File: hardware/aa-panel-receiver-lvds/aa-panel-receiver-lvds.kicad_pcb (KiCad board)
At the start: 2 copper layers, 95.4 x 54 mm, 96 parts, among them CN101 Conn_01x02, CN102 Conn_01x02, CN201 8P8C, CN202 Conn_01x08, CN251 Conn_01x08, CN301 8P8C, CN302 Conn_01x08, CN351 Conn_01x08, U101 CRE1S0505S3C, U201 ST26C32, U202 Si8640EB-B-IU, U301 ST26C32, U302 Si8640EB-B-IU

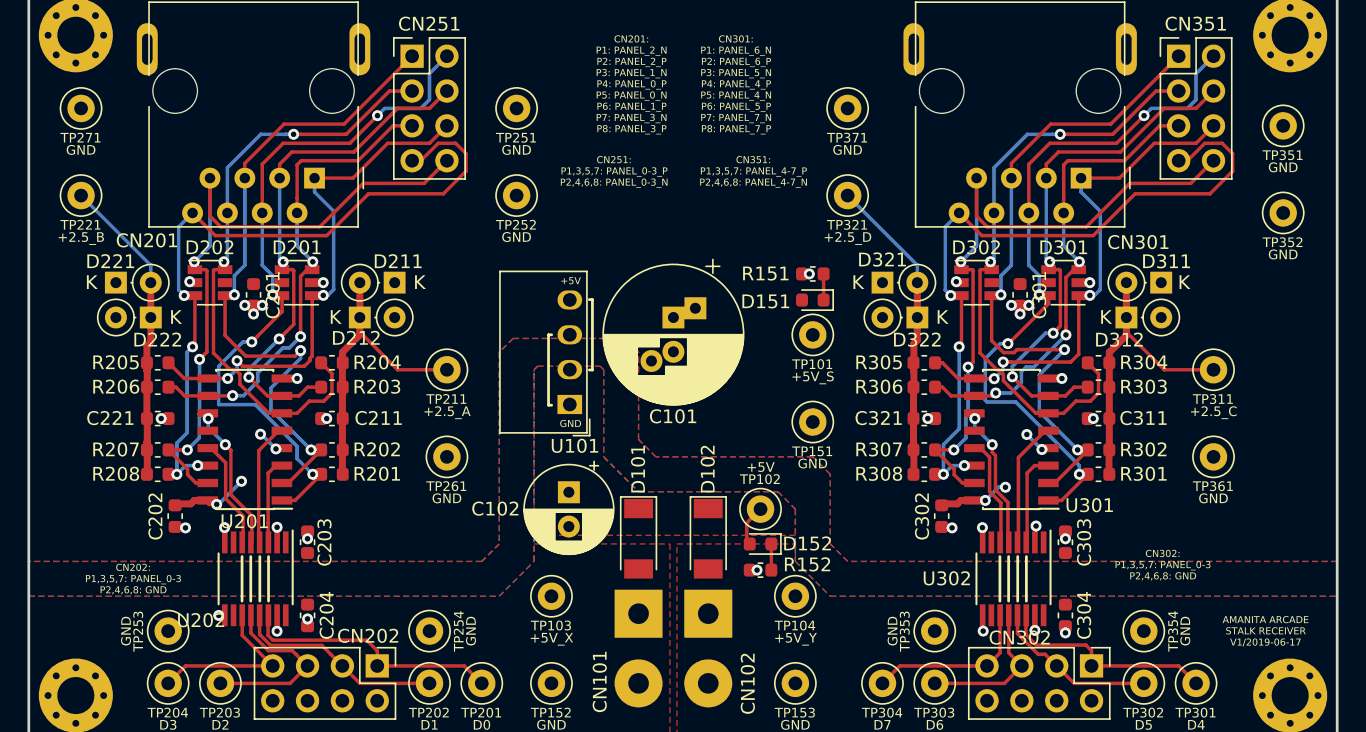
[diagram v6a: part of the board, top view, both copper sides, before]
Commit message: Final designs and actual sent gerbers for first for-real run
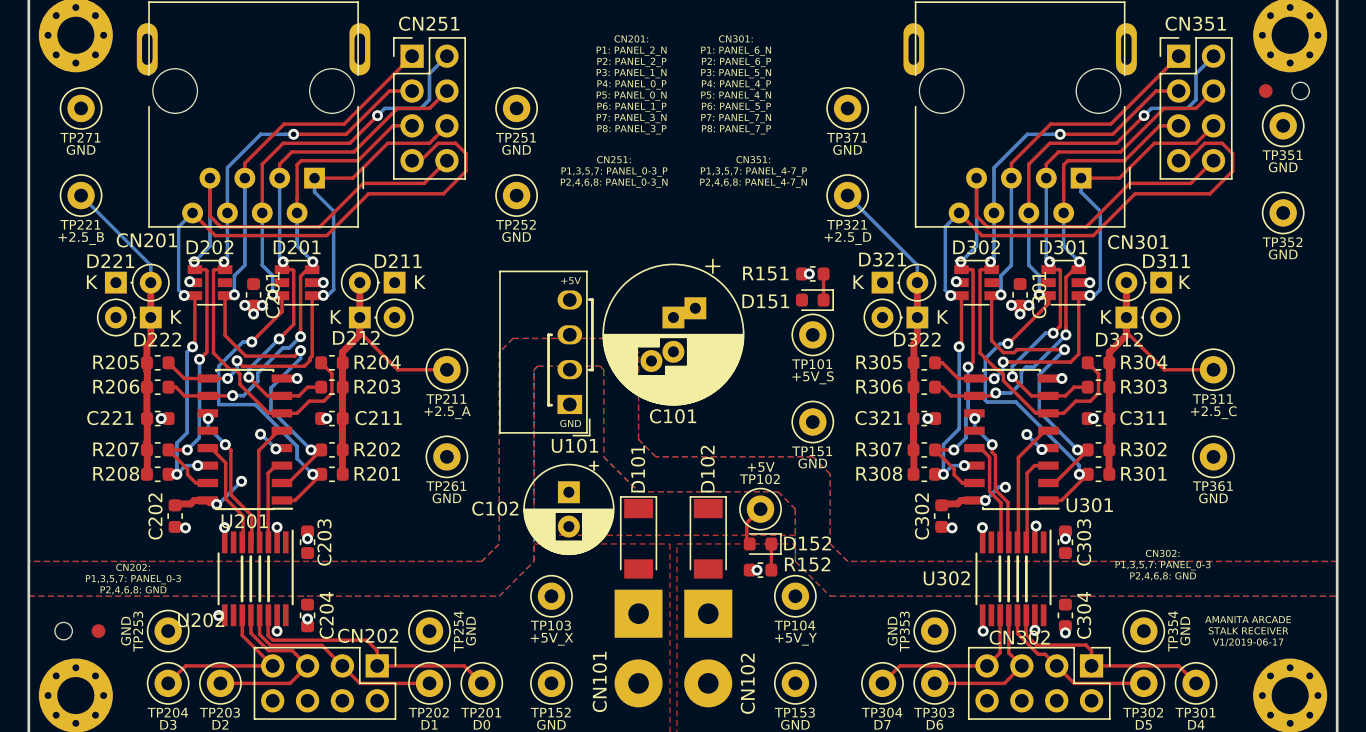
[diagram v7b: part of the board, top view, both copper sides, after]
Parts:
- added FD1: Fiducial, Fiducial:Fiducial_1mm_Dia_2.54mm_Outer_CopperTop, F.Cu at (96.5, 96.5)
- added FD2: Fiducial, Fiducial:Fiducial_1mm_Dia_2.54mm_Outer_CopperTop, F.Cu at (181.6, 57.1)
- added FD5: Fiducial, aa-shared:StencilAlignment_1.27mm, F.Cu at (94.0, 96.5)
- added FD6: Fiducial, aa-shared:StencilAlignment_1.27mm, F.Cu at (184.2, 57.1)
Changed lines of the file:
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@@
     (tracks 742)
     (zones 0)
-    (modules 96)
+    (modules 100)
     (nets 47)
   )
@@
     (uvia_drill 0.1)
   )
+  (module aa-shared:StencilAlignment_1.27mm (layer F.Cu)
+    (at 184.15 57.15)
+    (fp_text reference FD6 (at 0 -2.032) (layer F.SilkS) hide
+      (effects (font (size 1 1) (thickness 0.15)))
+    )
+    (fp_text value Fiducial (at 0 2.667) (layer F.Fab)
+      (effects (font (size 1 1) (thickness 0.15)))
+    )
+    (pad "" np_thru_hole circle (at 0 0) (size 1.27 1.27) (drill 1.27) (layers *.Cu *.Paste *.Mask)
+      (solder_paste_margin 0.00254))
+  )
+  (module Fiducial:Fiducial_1mm_Dia_2.54mm_Outer_CopperTop (layer F.Cu)
+    (at 181.61 57.15)
+    (descr "Circular Fiducial, 1mm bare copper top, 2.54mm keepout")
+    (tags fiducial)
+    (attr smd)
+    (fp_text reference FD2 (at 0 -2.5) (layer F.SilkS) hide
+      (effects (font (size 1 1) (thickness 0.15)))
+    )
+    (fp_text value Fiducial (at 0 2.5) (layer F.Fab)
+      (effects (font (size 1 1) (thickness 0.15)))
+    )
+    (fp_text user %R (at 0 0) (layer F.Fab)
+      (effects (font (size 1 1) (thickness 0.15)))
+    )
+    (fp_circle (center 0 0) (end 1.55 0) (layer F.CrtYd) (width 0.05))
+    (pad "" smd circle (at 0 0) (size 1 1) (layers F.Cu F.Mask)
+      (solder_mask_margin 0.77) (clearance 0.77))
+  )
   (module aa-shared:TestPoint_Loop_D1.80mm_Drill1.0mm_Beaded (layer F.Cu)
     (at 147.32 93.98)
@@
     )
   )
+  (module Fiducial:Fiducial_1mm_Dia_2.54mm_Outer_CopperTop (layer F.Cu)
+    (at 96.52 96.52)
+    (descr "Circular Fiducial, 1mm bare copper top, 2.54mm keepout")
+    (tags fiducial)
+    (attr smd)
+    (fp_text reference FD1 (at 0 -2.5) (layer F.SilkS) hide
+      (effects (font (size 1 1) (thickness 0.15)))
+    )
+    (fp_text value Fiducial (at 0 2.5) (layer F.Fab)
+      (effects (font (size 1 1) (thickness 0.15)))
+    )
+    (fp_circle (center 0 0) (end 1.55 0) (layer F.CrtYd) (width 0.05))
+    (fp_text user %R (at 0 0) (layer F.Fab)
+      (effects (font (size 1 1) (thickness 0.15)))
+    )
+    (pad "" smd circle (at 0 0) (size 1 1) (layers F.Cu F.Mask)
+      (solder_mask_margin 0.77) (clearance 0.77))
+  )
+  (module aa-shared:StencilAlignment_1.27mm (layer F.Cu)
+    (at 93.98 96.52)
+    (fp_text reference FD5 (at 0 -2.032) (layer F.SilkS) hide
+      (effects (font (size 1 1) (thickness 0.15)))
+    )
+    (fp_text value Fiducial (at 0 2.667) (layer F.Fab)
+      (effects (font (size 1 1) (thickness 0.15)))
+    )
+    (pad "" np_thru_hole circle (at 0 0) (size 1.27 1.27) (drill 1.27) (layers *.Cu *.Paste *.Mask)
+      (solder_paste_margin 0.00254))
+  )
   (gr_text +5V (at 130.937 70.993) (layer F.SilkS)
     (effects (font (size 0.508 0.508) (thickness 0.0762)))
@@
   )
   (gr_line (start 162.2298 91.0844) (end 162.2298 94.3356) (layer F.SilkS) (width 0.2))
-  (gr_text "AMANITA ARCADE\nSTALK RECEIVER\nV1/2019-06-17" (at 181.61 96.52) (layer F.SilkS)
+  (gr_text "AMANITA ARCADE\nSTALK RECEIVER\nV1/2019-06-17" (at 180.34 96.52) (layer F.SilkS)
     (effects (font (size 0.508 0.508) (thickness 0.0762)))
   )

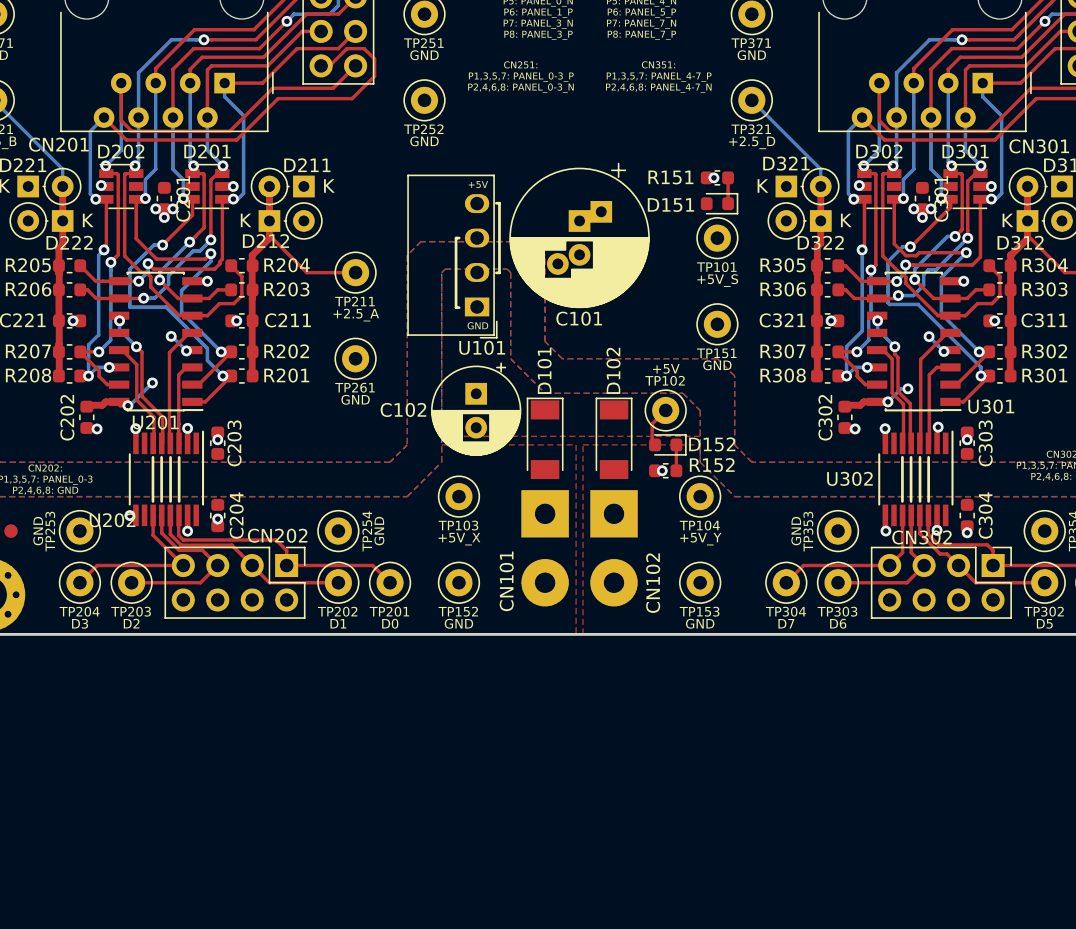
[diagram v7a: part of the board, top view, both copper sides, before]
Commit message: Minor board updates to fix issues discovered during build
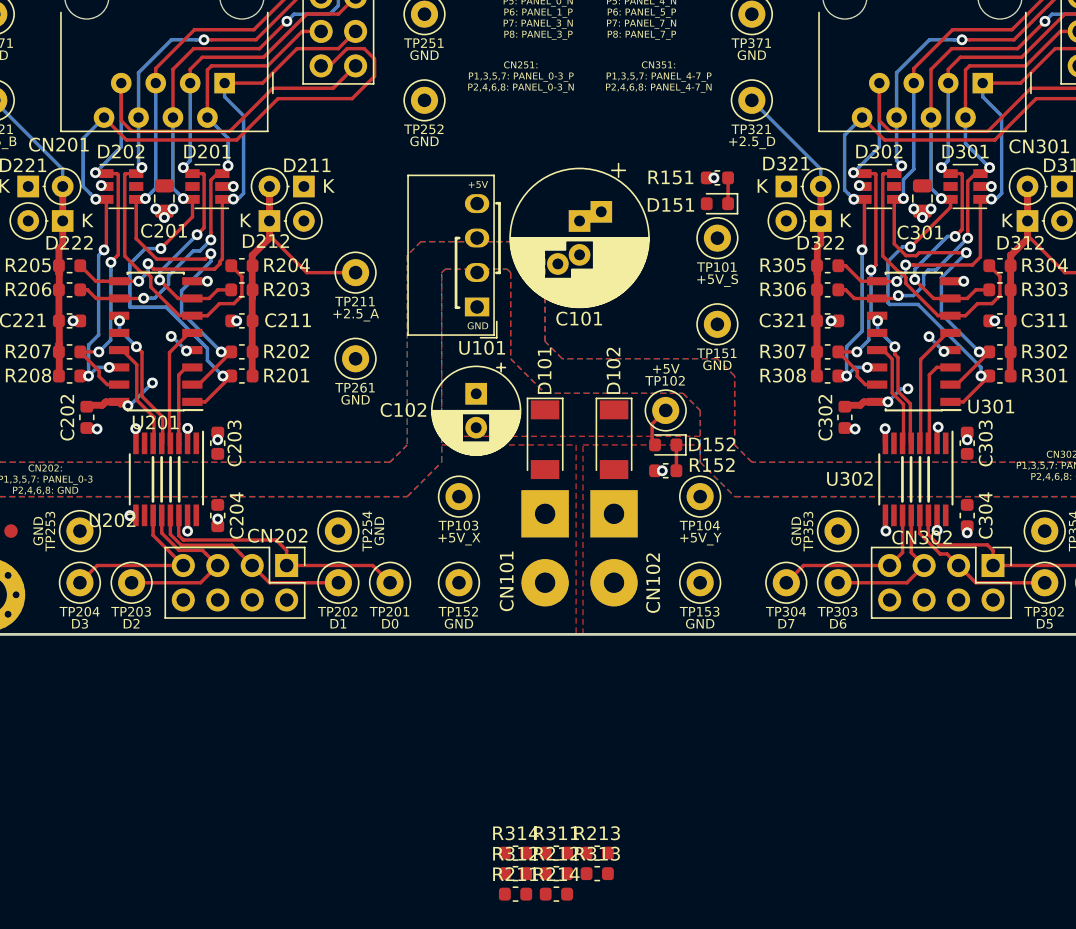
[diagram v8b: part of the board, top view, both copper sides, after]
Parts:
- added R211: 120, Resistor_SMD:R_0603_1608Metric, F.Cu at (133.7, 123.3)
- added R212: 120, Resistor_SMD:R_0603_1608Metric, F.Cu at (136.7, 121.8)
- added R213: 120, Resistor_SMD:R_0603_1608Metric, F.Cu at (139.7, 120.3)
- added R214: 120, Resistor_SMD:R_0603_1608Metric, F.Cu at (136.7, 123.3)
- added R311: 120, Resistor_SMD:R_0603_1608Metric, F.Cu at (136.7, 120.3)
- added R312: 120, Resistor_SMD:R_0603_1608Metric, F.Cu at (133.7, 121.8)
- added R313: 120, Resistor_SMD:R_0603_1608Metric, F.Cu at (139.7, 121.8)
- added R314: 120, Resistor_SMD:R_0603_1608Metric, F.Cu at (133.7, 120.3)
- C201, C301: footprint Capacitor_SMD:C_0603_1608Metric -> Capacitor_SMD:C_0805_2012Metric
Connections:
- CN202 pad 1: /PANEL_0 -> Net-(CN202-Pad1)
- CN202 pad 3: /PANEL_1 -> Net-(CN202-Pad3)
- CN202 pad 5: /PANEL_2 -> Net-(CN202-Pad5)
- CN202 pad 7: /PANEL_3 -> Net-(CN202-Pad7)
- CN302 pad 1: /PANEL_4 -> Net-(CN302-Pad1)
- CN302 pad 3: /PANEL_5 -> Net-(CN302-Pad3)
- CN302 pad 5: /PANEL_6 -> Net-(CN302-Pad5)
- CN302 pad 7: /PANEL_7 -> Net-(CN302-Pad7)
- TP201 pad 1: /PANEL_0 -> Net-(CN202-Pad1)
- TP202 pad 1: /PANEL_1 -> Net-(CN202-Pad3)
- TP203 pad 1: /PANEL_2 -> Net-(CN202-Pad5)
- TP204 pad 1: /PANEL_3 -> Net-(CN202-Pad7)
- TP301 pad 1: /PANEL_4 -> Net-(CN302-Pad1)
- TP302 pad 1: /PANEL_5 -> Net-(CN302-Pad3)
- TP303 pad 1: /PANEL_6 -> Net-(CN302-Pad5)
- TP304 pad 1: /PANEL_7 -> Net-(CN302-Pad7)
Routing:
- net /PANEL_3_N: track 49.7 -> 50.8 mm
- net /PANEL_7_N: track 49.7 -> 50.8 mm
- net /PANEL_6_P: track 35.1 -> 35.7 mm
